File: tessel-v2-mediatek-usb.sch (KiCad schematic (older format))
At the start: 51 parts

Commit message: still refactoring. usb is a pain
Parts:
- removed C? (x3): 100nF, tm-kicad-lib:SMD-0402-C, symbol C
- removed C? (x3): 10uF, SMD_Packages:SMD-0805, symbol C
- removed C?: 100pF, tm-kicad-lib:SMD-0402-C, symbol C
- removed D? (x3): PRTR5V0U2X,215, tm-kicad-lib:PRTR5V0U2X,215, symbol PRTR5V0U2X,215
- removed J?: USB_A_2_stack, tm-kicad-lib:USB-double-xx-UAF-28, symbol USB_A_2_stack
- removed L? (x3): BLM21PG221SN1D, SMD_Packages:SMD-0805, symbol INDUCTOR
- removed R? (x3): 100kR, tm-kicad-lib:SMD-0402-R, symbol R
- removed U?: AIC1528-0PSTR, tm-kicad-lib:SOP-8, symbol AIC1528-0PSTR
- added C? (x3): 100nF, tm-kicad-lib:SMD-0402-C, symbol C
- added C? (x3): 10uF, SMD_Packages:SMD-0805, symbol C
- added D? (x3): PRTR5V0U2X,215, tm-kicad-lib:PRTR5V0U2X,215, symbol PRTR5V0U2X,215
- added L? (x3): BLM21PG221SN1D, SMD_Packages:SMD-0805, symbol INDUCTOR
- added R? (x2): 100kR, tm-kicad-lib:SMD-0402-R, symbol R
- added U?: AIC1528-0PSTR, tm-kicad-lib:SOP-8, symbol AIC1528-0PSTR
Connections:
- wire segments 286 -> 212
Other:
- moved on the sheet: C?, D?, J?, L?, R?, U?

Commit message: last but not least: refactoring mediatek itself
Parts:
- removed C?: 100pF, tm-kicad-lib:SMD-0402-C, symbol C
- removed D? (x2): PRTR5V0U2X,215, tm-kicad-lib:PRTR5V0U2X,215, symbol PRTR5V0U2X,215
- removed J?: USB_A_2_stack, tm-kicad-lib:USB-double-xx-UAF-28, symbol USB_A_2_stack
- removed R? (x2): 100kR, tm-kicad-lib:SMD-0402-R, symbol R
- removed R?: 1R DNP, tm-kicad-lib:SMD-0603-R, symbol R
- added C? (x2): 100pF, tm-kicad-lib:SMD-0402-C, symbol C
- added D? (x2): PRTR5V0U2X,215, tm-kicad-lib:PRTR5V0U2X,215, symbol PRTR5V0U2X,215
- added J? (x2): USB_A_2_stack, tm-kicad-lib:USB-double-xx-UAF-28, symbol USB_A_2_stack
- added R? (x2): 100kR, tm-kicad-lib:SMD-0402-R, symbol R
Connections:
- net labels added: USB_PU
- net labels removed: +1.8V, BUS_B, XRSTJ
- wire segments 212 -> 268
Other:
- note removed: "externally regulated to 3.3v"
- note removed: "load cap derated from 20pF"
- moved on the sheet: C?, D?, L?, R?, U?, U?F, X?

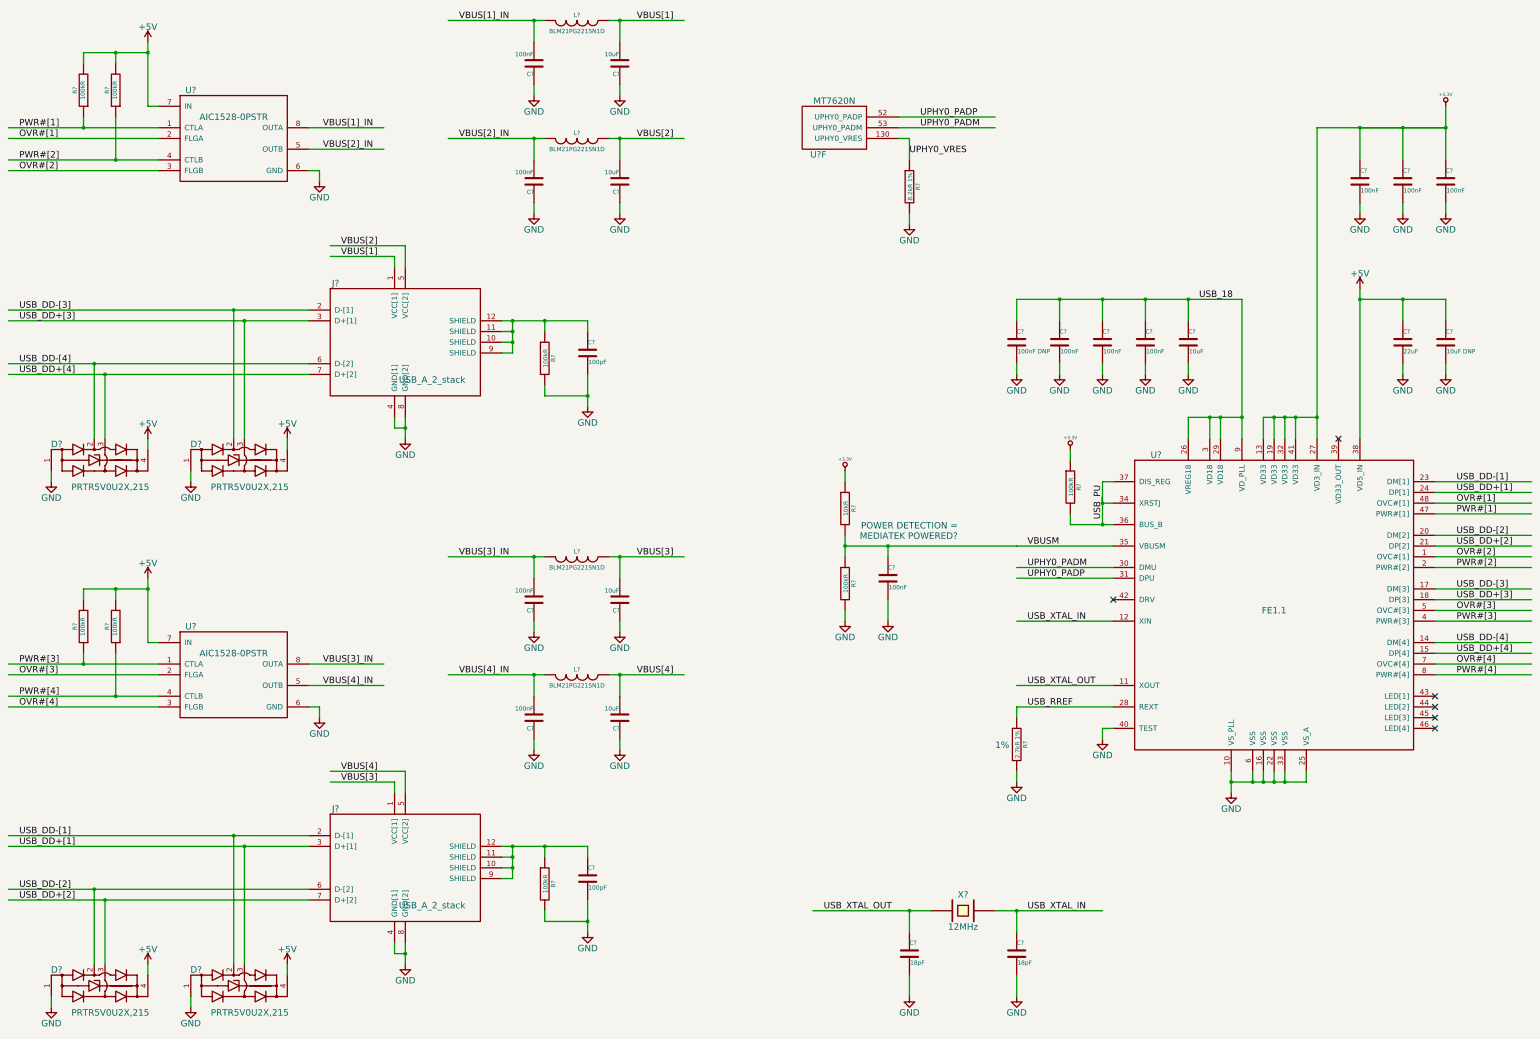
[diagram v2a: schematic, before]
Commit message: reset annotation
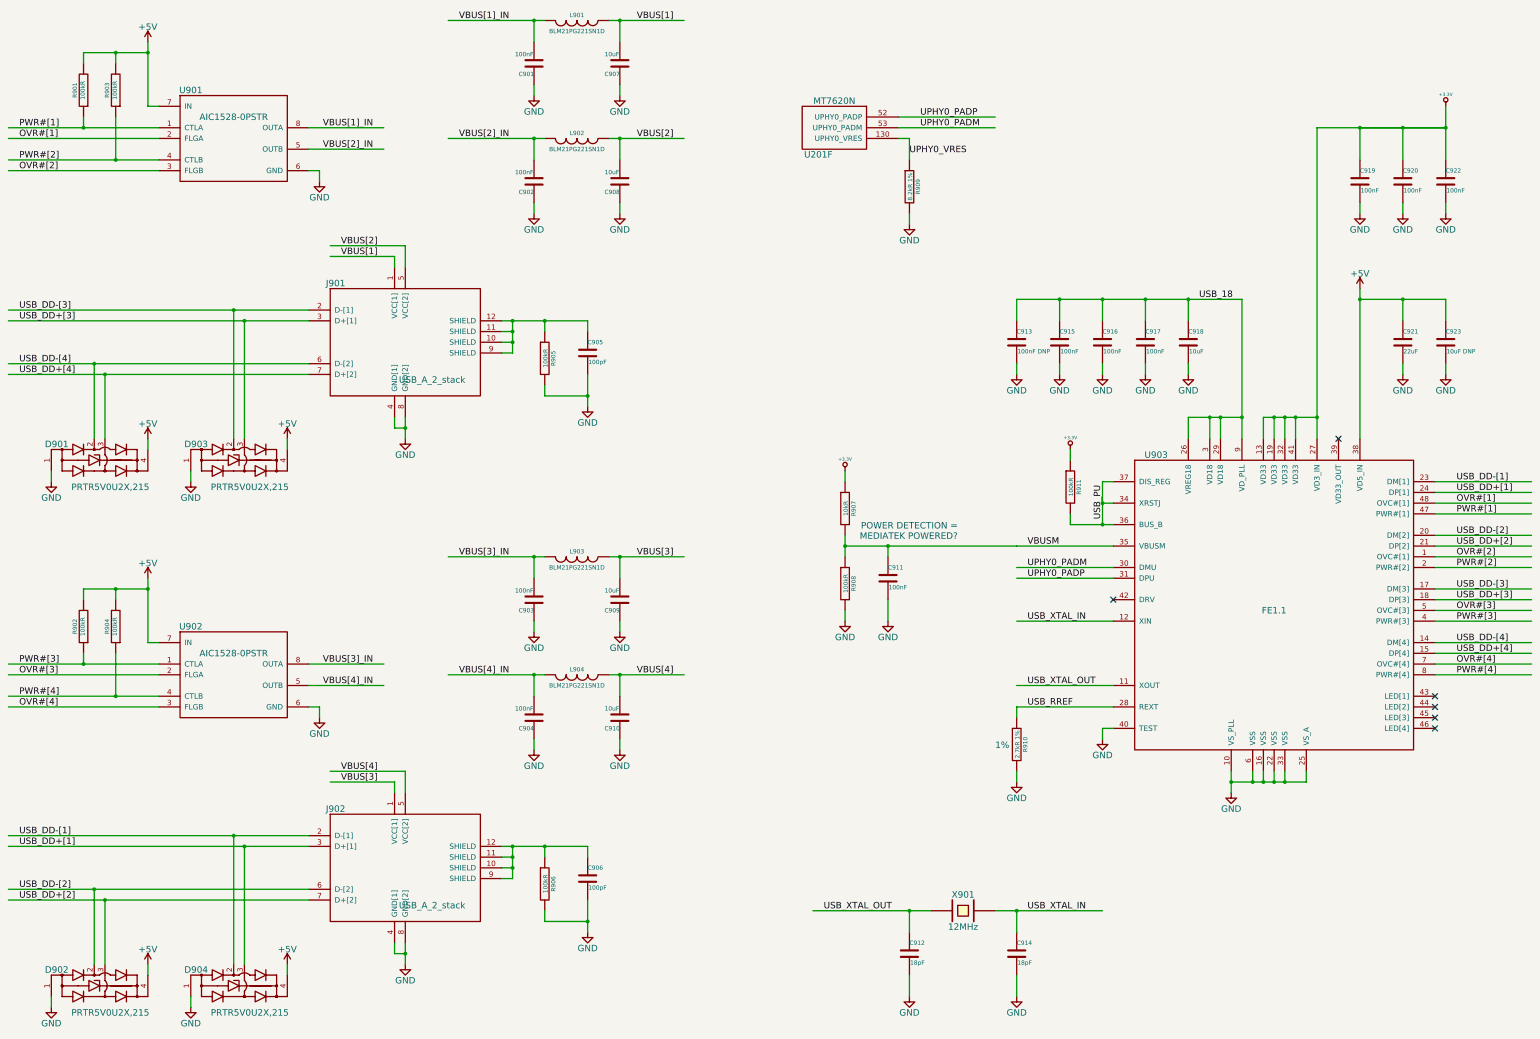
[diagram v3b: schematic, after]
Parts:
- gave numbers to parts that had none: 49

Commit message: annotation did not take?
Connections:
- wire segments 268 -> 202
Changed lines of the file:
@@
 	2300 6800 2300 7200
 Wire Wire Line
-	2600 6100 2600 6200
-Wire Wire Line
-	2600 6200 2600 6700
+	2600 6100 2600 6700
 Wire Wire Line
 	2000 6200 2000 6300
@@
 	14300 4200 14300 4100
 Wire Wire Line
-	13900 3500 14300 3500
-Wire Wire Line
-	14300 3500 14700 3500
+	13900 3500 14700 3500
 Wire Wire Line
 	10700 9200 10700 9400
 Wire Wire Line
-	1300 6900 2000 6900
-Wire Wire Line
-	2000 6900 2700 6900
+	1300 6900 2700 6900
 Wire Wire Line
 	2700 7000 1300 7000
 Wire Wire Line
-	1300 7200 2300 7200
-Wire Wire Line
-	2300 7200 2700 7200
+	1300 7200 2700 7200
 Wire Wire Line
 	2700 7300 1300 7300
 Wire Wire Line
-	5400 7000 6200 7000
-Wire Wire Line
-	6200 7000 6300 7000
+	5400 7000 6300 7000
 Wire Wire Line
 	6200 7000 6200 7200
@@
 Connection ~ 2300 6200
 Wire Wire Line
-	6900 7000 7000 7000
-Wire Wire Line
-	7000 7000 7600 7000
+	6900 7000 7600 7000
 Connection ~ 6200 7000
 Connection ~ 7000 7000
@@
 	7000 7700 7000 7600
 Wire Wire Line
-	5400 5900 6200 5900
-Wire Wire Line
-	6200 5900 6300 5900
+	5400 5900 6300 5900
 Wire Wire Line
 	6200 5900 6200 6100
@@
 	7000 6100 7000 5900
 Wire Wire Line
-	6900 5900 7000 5900
-Wire Wire Line
-	7000 5900 7600 5900
+	6900 5900 7600 5900
 Connection ~ 6200 5900
 Connection ~ 7000 5900
@@
 	2600 6700 2700 6700
 Wire Wire Line
-	2000 6200 2300 6200
-Wire Wire Line
-	2300 6200 2600 6200
+	2000 6200 2600 6200
 Connection ~ 2600 6200
 Connection ~ 2000 1900
@@
 	2300 1800 2300 2200
 Wire Wire Line
-	2600 1100 2600 1200
-Wire Wire Line
-	2600 1200 2600 1700
+	2600 1100 2600 1700
 Wire Wire Line
 	2000 1200 2000 1300
@@
 	2300 1200 2300 1300
 Wire Wire Line
-	1300 1900 2000 1900
-Wire Wire Line
-	2000 1900 2700 1900
+	1300 1900 2700 1900
 Wire Wire Line
 	2700 2000 1300 2000
 Wire Wire Line
-	1300 2200 2300 2200
-Wire Wire Line
-	2300 2200 2700 2200
+	1300 2200 2700 2200
 Wire Wire Line
 	2700 2300 1300 2300
 Wire Wire Line
-	5400 2000 6200 2000
-Wire Wire Line
-	6200 2000 6300 2000
+	5400 2000 6300 2000
 Wire Wire Line
 	6200 2000 6200 2200
@@
 Connection ~ 2300 1200
 Wire Wire Line
-	6900 2000 7000 2000
-Wire Wire Line
-	7000 2000 7600 2000
+	6900 2000 7600 2000
 Connection ~ 6200 2000
 Connection ~ 7000 2000
@@
 	7000 2700 7000 2600
 Wire Wire Line
-	5400 900  6200 900
-Wire Wire Line
-	6200 900  6300 900
+	5400 900  6300 900
 Wire Wire Line
 	6200 900  6200 1100
@@
 	7000 1100 7000 900
 Wire Wire Line
-	6900 900  7000 900
-Wire Wire Line
-	7000 900  7600 900
+	6900 900  7600 900
 Connection ~ 6200 900
 Connection ~ 7000 900
@@
 	2600 1700 2700 1700
 Wire Wire Line
-	2000 1200 2300 1200
-Wire Wire Line
-	2300 1200 2600 1200
+	2000 1200 2600 1200
 Connection ~ 2600 1200
 Wire Wire Line
@@
 	14700 3500 14700 3700
 Wire Wire Line
-	13900 3400 13900 3500
-Wire Wire Line
-	13900 3500 13900 4800
+	13900 3400 13900 4800
 Connection ~ 13900 3500
 Wire Wire Line
@@
 	10700 3700 10700 3500
 Wire Wire Line
-	10700 3500 11100 3500
-Wire Wire Line
-	11100 3500 11500 3500
-Wire Wire Line
-	11500 3500 11900 3500
-Wire Wire Line
-	11900 3500 12300 3500
-Wire Wire Line
-	12300 3500 12800 3500
+	10700 3500 12800 3500
 Wire Wire Line
 	12300 3500 12300 3700
@@
 	14700 2700 14700 2600
 Wire Wire Line
-	14700 1700 14700 1900
+	14700 1700 14700 2200
 Wire Wire Line
 	13900 1900 13900 2200
 Wire Wire Line
-	13900 1900 14300 1900
-Wire Wire Line
-	14300 1900 14700 1900
-Wire Wire Line
-	14700 1900 14300 1900
-Wire Wire Line
-	14300 1900 13900 1900
-Wire Wire Line
-	13900 1900 13500 1900
-Wire Wire Line
-	13000 4600 13100 4600
-Wire Wire Line
-	13100 4600 13200 4600
-Wire Wire Line
-	13200 4600 13300 4600
-Wire Wire Line
-	13300 4600 13500 4600
-Wire Wire Line
-	13500 1900 13500 4600
-Wire Wire Line
-	13500 4600 13500 4800
+	13500 1900 14700 1900
+Wire Wire Line
+	13000 4600 13500 4600
+Wire Wire Line
+	13500 1900 13500 4800
 Wire Wire Line
 	13300 4800 13300 4600
@@
 	13100 4800 13100 4600
 Connection ~ 13100 4600
-Wire Wire Line
-	14700 2200 14700 1900
 Wire Wire Line
 	14300 1900 14300 2200
@@
 	11200 5500 11200 5600
 Wire Wire Line
-	11200 5600 11500 5600
-Wire Wire Line
-	11500 5600 11600 5600
-Wire Wire Line
-	11500 5200 11500 5400
-Wire Wire Line
-	11500 5400 11500 5600
+	11200 5600 11600 5600
+Wire Wire Line
+	11500 5200 11500 5600
 Connection ~ 11500 5600
 Wire Wire Line
@@
 	10700 8000 10700 7900
 Wire Wire Line
-	11600 5800 10700 5800
+	9100 5800 11600 5800
 Wire Wire Line
 	11600 6000 10700 6000
@@
 	11600 6100 10700 6100
 Wire Wire Line
-	12800 3500 12800 4600
+	12800 3500 12800 4800
 Wire Wire Line
 	12300 4600 12300 4800
 Wire Wire Line
-	12800 4600 12800 4800
-Wire Wire Line
-	12300 4600 12500 4600
-Wire Wire Line
-	12500 4600 12600 4600
-Wire Wire Line
-	12600 4600 12800 4600
+	12300 4600 12800 4600
 Connection ~ 12800 4600
 Wire Wire Line
@@
 	11500 7500 11600 7500
 Wire Wire Line
-	10500 9200 10700 9200
-Wire Wire Line
-	10700 9200 11500 9200
+	10500 9200 11500 9200
 Connection ~ 10700 9200
 Wire Wire Line
@@
 	9700 10000 9700 9800
 Wire Wire Line
-	8800 9200 9700 9200
-Wire Wire Line
-	9700 9200 9900 9200
+	8800 9200 9900 9200
 Wire Wire Line
 	9700 9400 9700 9200
 Connection ~ 9700 9200
 Wire Wire Line
-	9100 5700 9100 5800
-Wire Wire Line
-	9100 5800 9100 5900
-Wire Wire Line
-	9100 5800 9500 5800
-Wire Wire Line
-	9500 5800 10700 5800
+	9100 5700 9100 5900
 Wire Wire Line
 	9500 5800 9500 5900
@@
 Connection ~ 6300 8600
 Wire Wire Line
-	5900 8600 6000 8600
-Wire Wire Line
-	6000 8600 6300 8600
-Wire Wire Line
-	6300 8600 6700 8600
+	5900 8600 6700 8600
 Wire Wire Line
 	6700 8600 6700 8700
@@
 	6300 9200 6300 9300
 Wire Wire Line
-	6700 9100 6700 9300
-Wire Wire Line
-	6700 9300 6700 9400
+	6700 9100 6700 9400
 Wire Wire Line
 	4900 9500 4900 9600
@@
 	4900 9600 5000 9600
 Wire Wire Line
-	5000 9500 5000 9600
-Wire Wire Line
-	5000 9600 5000 9700
+	5000 9500 5000 9700
 Connection ~ 5000 9600
 Wire Wire Line
@@
 Connection ~ 6000 8800
 Wire Wire Line
-	6000 8600 6000 8700
-Wire Wire Line
-	6000 8700 6000 8800
-Wire Wire Line
-	6000 8800 6000 8900
+	6000 8600 6000 8900
 Wire Wire Line
 	6300 8600 6300 8700
@@
 	5000 7900 5000 8100
 Wire Wire Line
-	1300 8500 3400 8500
-Wire Wire Line
-	3400 8500 4100 8500
-Wire Wire Line
-	1300 8600 3500 8600
-Wire Wire Line
-	3500 8600 4100 8600
-Wire Wire Line
-	1300 9000 2100 9000
-Wire Wire Line
-	2100 9000 4100 9000
-Wire Wire Line
-	1300 9100 2200 9100
-Wire Wire Line
-	2200 9100 4100 9100
+	1300 8500 4100 8500
+Wire Wire Line
+	1300 8600 4100 8600
+Wire Wire Line
+	1300 9000 4100 9000
+Wire Wire Line
+	1300 9100 4100 9100
 Wire Wire Line
 	2100 9700 2100 9000
@@
 Connection ~ 6300 3700
 Wire Wire Line
-	5900 3700 6000 3700
-Wire Wire Line
-	6000 3700 6300 3700
-Wire Wire Line
-	6300 3700 6700 3700
+	5900 3700 6700 3700
 Wire Wire Line
 	6700 3700 6700 3800
@@
 	6300 4300 6300 4400
 Wire Wire Line
-	6700 4200 6700 4400
-Wire Wire Line
-	6700 4400 6700 4500
+	6700 4200 6700 4500
 Wire Wire Line
 	4900 4600 4900 4700
@@
 	4900 4700 5000 4700
 Wire Wire Line
-	5000 4600 5000 4700
-Wire Wire Line
-	5000 4700 5000 4800
+	5000 4600 5000 4800
 Connection ~ 5000 4700
 Wire Wire Line
@@
 Connection ~ 6000 3900
 Wire Wire Line
-	6000 3700 6000 3800
-Wire Wire Line
-	6000 3800 6000 3900
-Wire Wire Line
-	6000 3900 6000 4000
+	6000 3700 6000 4000
 Wire Wire Line
 	6300 3700 6300 3800
@@
 	5000 3000 5000 3200
 Wire Wire Line
-	1300 3600 3400 3600
-Wire Wire Line
-	3400 3600 4100 3600
-Wire Wire Line
-	1300 3700 3500 3700
-Wire Wire Line
-	3500 3700 4100 3700
-Wire Wire Line
-	1300 4100 2100 4100
-Wire Wire Line
-	2100 4100 4100 4100
-Wire Wire Line
-	1300 4200 2200 4200
-Wire Wire Line
-	2200 4200 4100 4200
+	1300 3600 4100 3600
+Wire Wire Line
+	1300 3700 4100 3700
+Wire Wire Line
+	1300 4100 4100 4100
+Wire Wire Line
+	1300 4200 4100 4200
 Wire Wire Line
 	2100 4800 2100 4100
@@
 Connection ~ 3500 3700
 Wire Wire Line
-	12700 7900 12700 8000
-Wire Wire Line
-	12700 8000 12700 8100
-Wire Wire Line
-	12700 8000 12900 8000
-Wire Wire Line
-	12900 8000 13000 8000
-Wire Wire Line
-	13000 8000 13100 8000
-Wire Wire Line
-	13100 8000 13200 8000
-Wire Wire Line
-	13200 8000 13400 8000
+	12700 7900 12700 8100
+Wire Wire Line
+	12700 8000 13400 8000
 Wire Wire Line
 	13400 8000 13400 7900
